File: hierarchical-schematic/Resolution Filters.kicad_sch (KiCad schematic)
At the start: 59 parts, among them J501 Conn_Coaxial, J502 Conn_Coaxial, J503 Terminal Block, K501 G5V-1, K502 G5V-1, SW501 SW_SPST, T501 Transformer_1P_1S, T502 Transformer_1P_1S, Y501 10.7MHz, Y502 10.7MHz, Y503 10.7MHz, Y504 10.7MHz

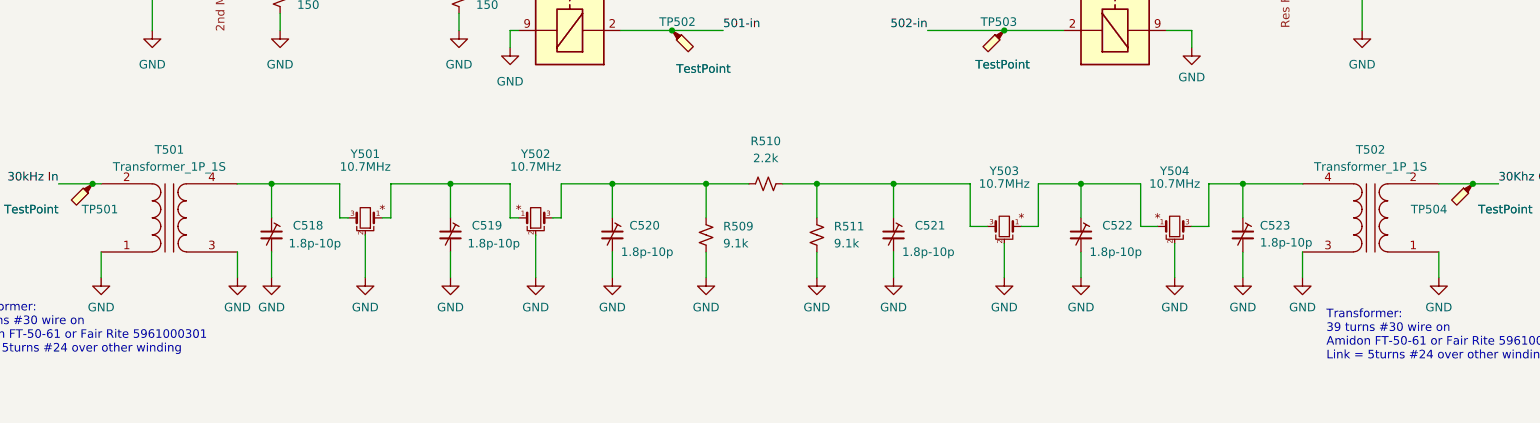
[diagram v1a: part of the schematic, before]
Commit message: updatess to kicad v8
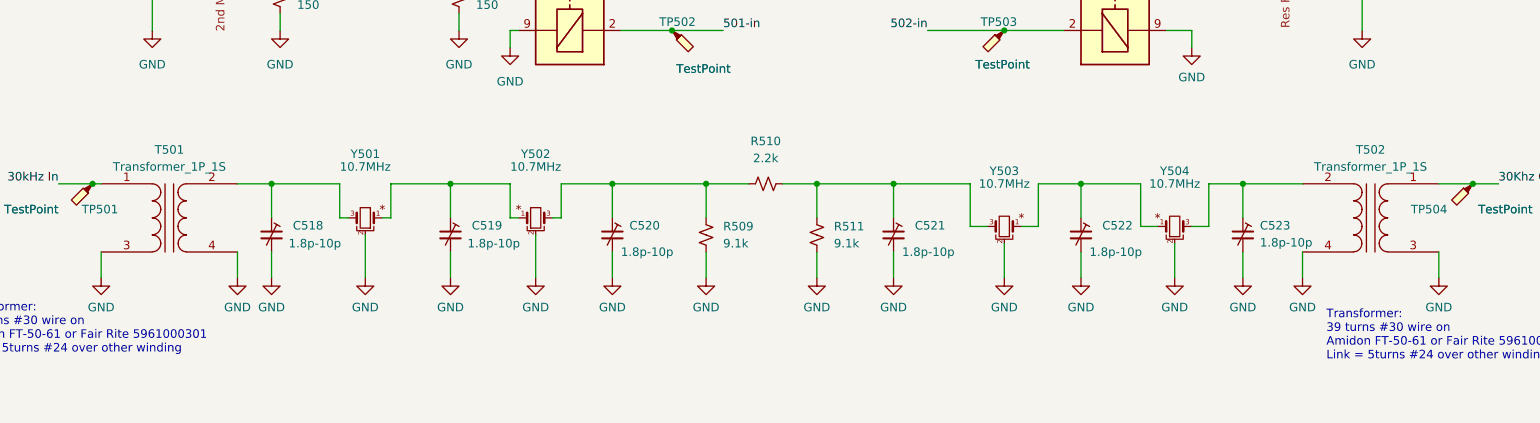
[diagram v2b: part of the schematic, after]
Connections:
- net 30Khz Out: now also T502.1 (AA); no longer T502.2 (AA)
- net 30kHz In: now also T501.1 (AA); no longer T501.2 (AA)
- net GND: now also T501.4 (SA), T502.4 (SA); no longer T501.1 (AB), T502.1 (AB)
- net at C518.1, Y501.3: now also T501.2 (SB); no longer T501.4 (SB)
- net at C523.1, Y504.3: now also T502.2 (SB); no longer T502.4 (SB)
